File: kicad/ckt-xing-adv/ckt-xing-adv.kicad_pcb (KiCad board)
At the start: 2 copper layers, 127 x 76.2 mm, 131 parts, among them J1 Screw_Terminal_01x02, J10 SM04B-SRSS, J11 SM04B-SRSS, J12 SM04B-SRSS, J13 Conn_02x03_Row_Letter_First, J14 Conn_02x03_Row_Letter_First, J15 Conn_02x05_Counter_Clockwise, J16 SM04B-SRSS, J17 Screw_Terminal_01x02, J18 Screw_Terminal_01x02, J2 Screw_Terminal_01x02, J3 Screw_Terminal_01x02, J4 SM04B-SRSS, J5 SM04B-SRSS, J6 SM04B-SRSS, J7 SM04B-SRSS, J8 SM04B-SRSS, J9 SM04B-SRSS, Q1 ZXMS6004FF, Q2 ZXMS6004FF, Q3 ZXMS6004FF, SW1 FSM4JSMATR, SW2 FSM4JSMATR, SW3 FSM4JSMATR, U1 AP7381-33Y, U2 AP63205WU, U3 W25Q128JVS, U4 ATtiny861A-S, U5 PCA9685PW, U6 PCA9555D, U7 PAM8301, U8 DRV8231A, U9 DRV8231A

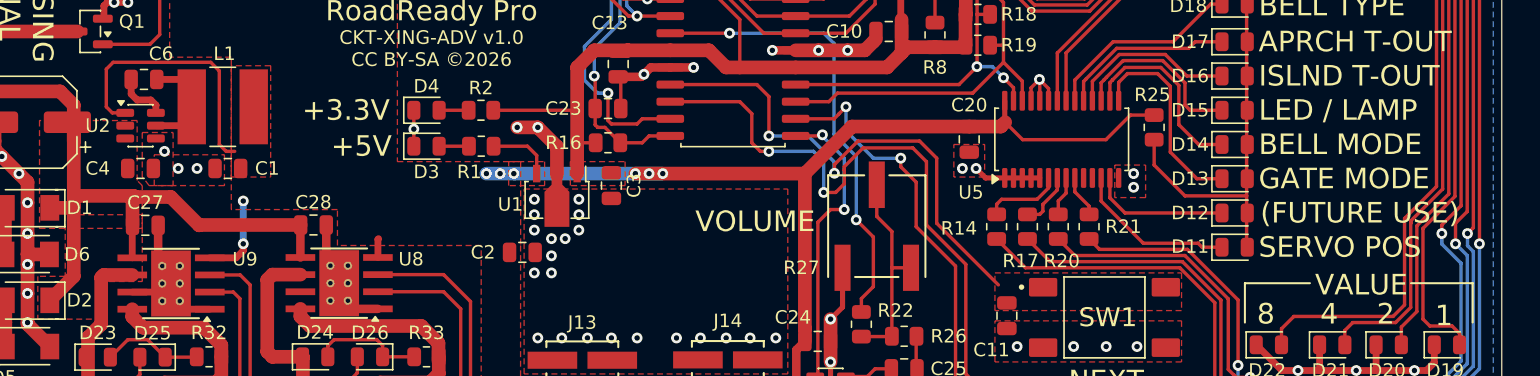
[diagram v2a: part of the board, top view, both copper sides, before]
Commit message: Updates to the big crossing - fix some actual DRC issues
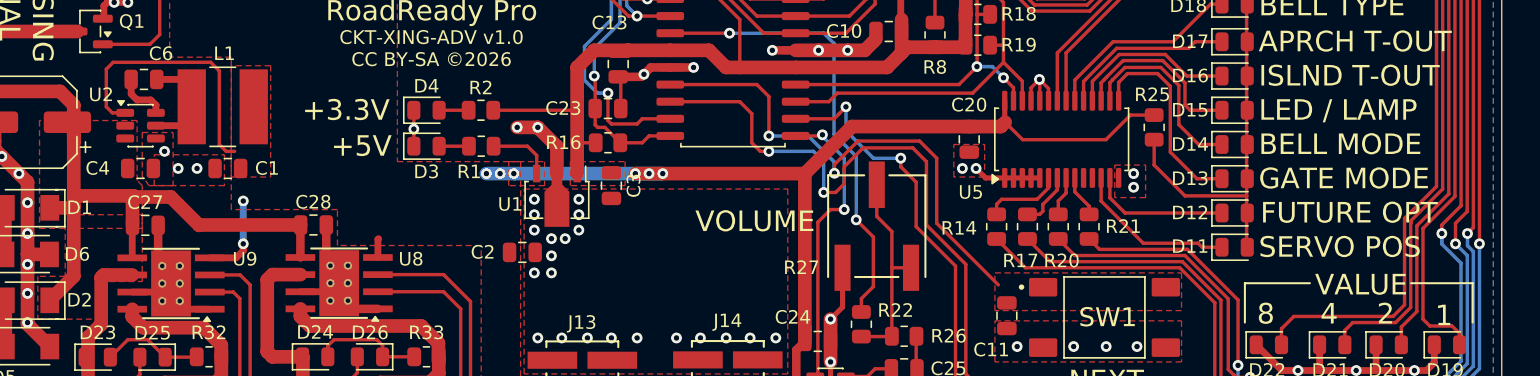
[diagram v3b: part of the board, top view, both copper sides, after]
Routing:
- net GND: track 160.5 -> 163.6 mm
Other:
- board text added: "FUTURE OPT"
- board text removed: "(FUTURE USE)"
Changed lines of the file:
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@@
 		(sheetname "/")
 		(sheetfile "ckt-xing-adv.kicad_sch")
-		(attr through_hole)
+		(attr smd)
 		(fp_line
 			(start -0.948813 2.9337)
@@
 		)
 		(embedded_fonts no)
+		(model "${ISE_3DMODELS}/Coilcraft-MSS6132.step"
+			(offset
+				(xyz 0 0 0)
+			)
+			(scale
+				(xyz 1 1 1)
+			)
+			(rotate
+				(xyz 90 -180 -90)
+			)
+		)
 	)
 	(footprint "Connector_JST:JST_SH_SM04B-SRSS-TB_1x04-1MP_P1.00mm_Horizontal"
@@
 		(sheetname "/")
 		(sheetfile "ckt-xing-adv.kicad_sch")
-		(attr through_hole)
+		(attr through_hole allow_missing_courtyard)
 		(fp_line
 			(start -2.62 3.62)
@@
 		)
 		(embedded_fonts no)
-		(model "${KICAD9_3DMODEL_DIR}/TerminalBlock_RND.3dshapes/TerminalBlock_RND_205-00012_1x02_P5.00mm_Horizontal.step"
+		(model "${ISE_3DMODELS}/Terminal_Block_2Pos_5mm.stp"
 			(offset
-				(xyz 0 0 0)
+				(xyz -2.54 -3.7338 0)
 			)
 			(scale
@@
 			)
 			(rotate
-				(xyz 0 0 0)
+				(xyz -0 -0 -0)
 			)
 		)
@@
 		(tags "TSOT TO_SOT_SMD")
 		(property "Reference" "U2"
-			(at -3.175 0 0)
+			(at -2.921 -2.286 0)
 			(layer "F.SilkS")
 			(effects
@@
 		)
 		(embedded_fonts no)
+		(model "${ISE_3DMODELS}/MOLEX_015910060.step"
+			(offset
+				(xyz 0 0 2.54)
+			)
+			(scale
+				(xyz 1 1 1)
+			)
+			(rotate
+				(xyz -90 -0 -0)
+			)
+		)
 	)
 	(footprint "LED_SMD:LED_0805_2012Metric"
@@
 		(sheetfile "ckt-xing-adv.kicad_sch")
 		(solder_mask_margin 0.07)
-		(attr smd)
 		(fp_line
 			(start -2.075 2.575)
@@
 		)
 		(embedded_fonts no)
-		(model "${KICAD9_3DMODEL_DIR}/TerminalBlock_RND.3dshapes/TerminalBlock_RND_205-00012_1x02_P5.00mm_Horizontal.step"
+		(model "${ISE_3DMODELS}/Terminal_Block_2Pos_5mm.stp"
 			(offset
-				(xyz 0 0 0)
+				(xyz -2.54 -3.7338 0)
 			)
 			(scale
@@
 			)
 			(rotate
-				(xyz 0 0 0)
+				(xyz -0 -0 -0)
 			)
 		)
@@
 		)
 		(embedded_fonts no)
+		(model "${ISE_3DMODELS}/FSM4JSMA.step"
+			(offset
+				(xyz 0 0 3.81)
+			)
+			(scale
+				(xyz 1 1 1)
+			)
+			(rotate
+				(xyz -0 -0 -90)
+			)
+		)
 	)
 	(footprint "LED_SMD:LED_0805_2012Metric"
@@
 			(layer "F.Fab")
 		)
+		(fp_circle
+			(center -2.54 -4.124999)
+			(end -2.159 -4.124999)
+			(stroke
+				(width 0.508)
+				(type solid)
+			)
+			(fill no)
+			(layer "F.Fab")
+		)
 		(fp_text user "${REFERENCE}"
 			(at 0 0 90)
@@
 		)
 		(embedded_fonts no)
+		(model "${ISE_3DMODELS}/MOLEX_015910060.step"
+			(offset
+				(xyz 0 0 2.54)
+			)
+			(scale
+				(xyz 1 1 1)
+			)
+			(rotate
+				(xyz -90 -0 -0)
+			)
+		)
 	)
 	(footprint "LED_SMD:LED_0805_2012Metric"
@@
 		(tags "THT terminal block RND 205-00012 pitch 5mm size 10x7.6mm drill 1.3mm pad 2.5mm")
 		(property "Reference" "J1"
-			(at -3.5284 -0.1316 180)
+			(at -3.5284 -0.1316 0)
 			(layer "F.SilkS")
 			(effects
@@
 		(sheetname "/")
 		(sheetfile "ckt-xing-adv.kicad_sch")
-		(attr through_hole)
+		(attr through_hole allow_missing_courtyard)
 		(fp_line
 			(start -2.62 3.62)
@@
 		)
 		(embedded_fonts no)
-		(model "${KICAD9_3DMODEL_DIR}/TerminalBlock_RND.3dshapes/TerminalBlock_RND_205-00012_1x02_P5.00mm_Horizontal.step"
+		(model "${ISE_3DMODELS}/Terminal_Block_2Pos_5mm.stp"
 			(offset
-				(xyz 0 0 0)
+				(xyz -2.54 -3.683 0)
 			)
 			(scale
@@
 			)
 			(rotate
-				(xyz 0 0 0)
+				(xyz -0 -0 -0)
 			)
 		)
@@
 		)
 		(embedded_fonts no)
-		(model "${KICAD9_3DMODEL_DIR}/TerminalBlock_RND.3dshapes/TerminalBlock_RND_205-00012_1x02_P5.00mm_Horizontal.step"
+		(model "${ISE_3DMODELS}/Terminal_Block_2Pos_5mm.stp"
 			(offset
-				(xyz 0 0 0)
+				(xyz -2.54 -3.7338 0)
 			)
 			(scale
@@
 			)
 			(rotate
-				(xyz 0 0 0)
+				(xyz -0 -0 -0)
 			)
 		)
@@
 		)
 		(embedded_fonts no)
+		(model "${ISE_3DMODELS}/FSM4JSMA.step"
+			(offset
+				(xyz 0 0 3.81)
+			)
+			(scale
+				(xyz 1 1 1)
+			)
+			(rotate
+				(xyz -0 -0 -90)
+			)
+		)
 	)
 	(footprint "ISE_UltraLibrarian:POT_3361P_BRN"
@@
 		)
 		(embedded_fonts no)
+		(model "${ISE_3DMODELS}/Bournes-3361P.step"
+			(offset
+				(xyz 1.905 -1.27 2.413)
+			)
+			(scale
+				(xyz 1 1 1)
+			)
+			(rotate
+				(xyz -0 -0 -180)
+			)
+		)
 	)
 	(footprint "Capacitor_SMD:C_0805_2012Metric"
@@
 		)
 		(embedded_fonts no)
+		(model "${ISE_3DMODELS}/FSM4JSMA.step"
+			(offset
+				(xyz 0 0 3.81)
+			)
+			(scale
+				(xyz 1 1 1)
+			)
+			(rotate
+				(xyz -0 -0 -90)
+			)
+		)
 	)
 	(footprint "Package_SO:TSSOP-28_4.4x9.7mm_P0.65mm"
@@
 		(tags "THT terminal block RND 205-00012 pitch 5mm size 10x7.6mm drill 1.3mm pad 2.5mm")
 		(property "Reference" "J2"
-			(at 7.453 -5.8825 180)
+			(at 7.453 -5.8825 0)
 			(layer "F.SilkS")
 			(effects
@@
 		)
 		(embedded_fonts no)
-		(model "${KICAD9_3DMODEL_DIR}/TerminalBlock_RND.3dshapes/TerminalBlock_RND_205-00012_1x02_P5.00mm_Horizontal.step"
+		(model "${ISE_3DMODELS}/Terminal_Block_2Pos_5mm.stp"
 			(offset
-				(xyz 0 0 0)
+				(xyz -2.54 -3.7338 0)
 			)
 			(scale
@@
 			)
 			(rotate
-				(xyz 0 0 0)
+				(xyz -0 -0 -0)
 			)
 		)
@@
 		(sheetfile "ckt-xing-adv.kicad_sch")
 		(solder_mask_margin 0.07)
-		(attr smd)
 		(fp_line
 			(start -2.075 2.575)
@@
 		)
 	)
-	(gr_text "(FUTURE USE)"
+	(gr_text "FUTURE OPT"
 		(at 134.493 70.231 0)
 		(layer "F.SilkS")
@@
 	)
 	(segment
+		(start 63.292 76.073)
+		(end 65.532 76.073)
+		(width 0.508)
+		(layer "F.Cu")
+		(net 5)
+	)
+	(segment
 		(start 68.834 40.259)
 		(end 71.501 40.259)
@@
 	)
 	(segment
+		(start 65.532 76.073)
+		(end 66.167 75.438)
+		(width 0.508)
+		(layer "F.Cu")
+		(net 5)
+	)
+	(segment
 		(start 50.4952 46.04375)
 		(end 49.4792 46.04375)
@@
 		(polygon
 			(pts
-				(xy 58.166 65.659) (xy 58.166 67.564) (xy 61.087 67.564) (xy 61.087 59.309) (xy 58.166 59.309) (xy 58.166 65.659)
+				(xy 58.166 65.659) (xy 58.166 67.564) (xy 61.087 67.564) (xy 61.087 59.309) (xy 58.166 59.309)
 			)
 		)

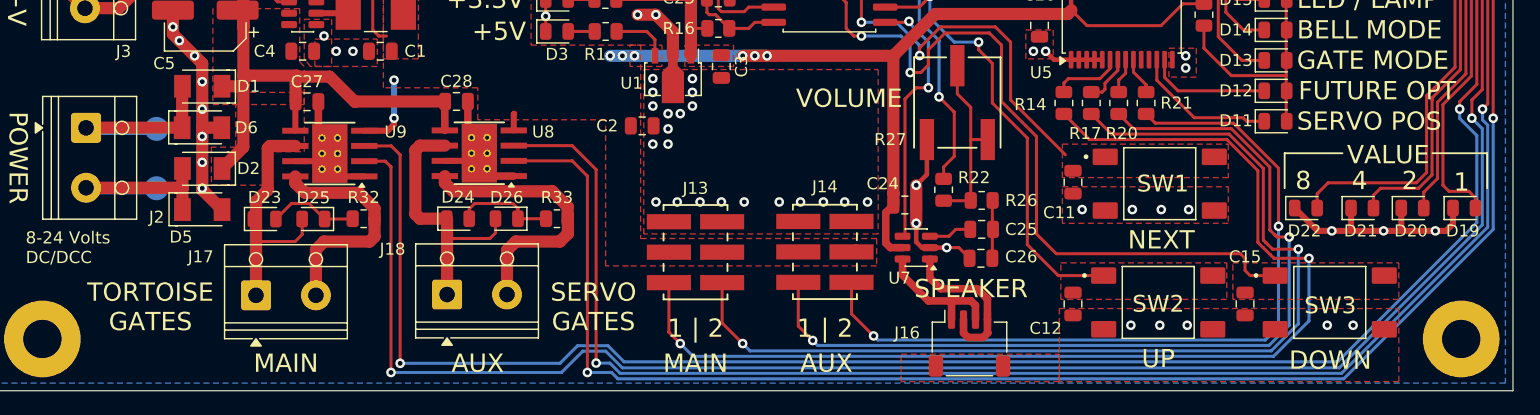
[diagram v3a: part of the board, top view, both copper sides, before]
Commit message: Add test points for servo outputs Feedback from Michael on text position, etc
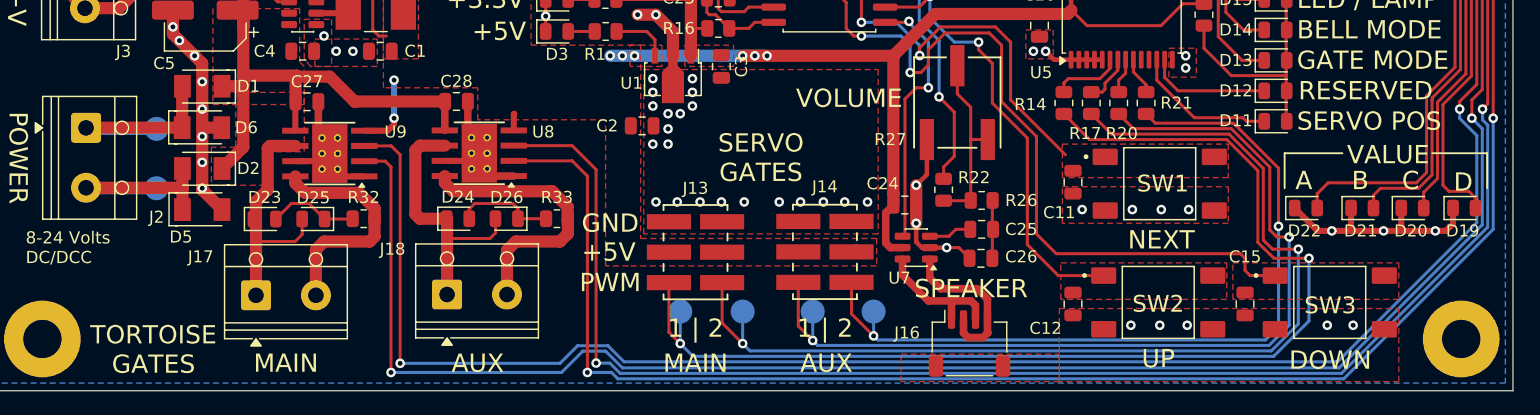
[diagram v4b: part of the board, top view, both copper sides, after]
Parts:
- added TP6: TestPoint, TestPoint:TestPoint_Pad_D2.0mm, B.Cu at (82.9, 88.6)
- added TP7: TestPoint, TestPoint:TestPoint_Pad_D2.0mm, B.Cu at (88.1, 88.6)
- added TP8: TestPoint, TestPoint:TestPoint_Pad_D2.0mm, B.Cu at (94.0, 88.6)
- added TP9: TestPoint, TestPoint:TestPoint_Pad_D2.0mm, B.Cu at (99.1, 88.6)
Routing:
- net Net-(J13-Pin_b1): track 85.0 -> 87.7 mm
- net Net-(J13-Pin_a1): track 93.8 -> 96.4 mm
- net Net-(J14-Pin_a1): track 74.9 -> 77.3 mm
- net Net-(J14-Pin_b1): track 65.8 -> 67.8 mm
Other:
- board text added: "A"
- board text added: "B"
- board text added: "D"
- board text added: "GND"
- board text added: "PWM"
- board text added: "RESERVED"
- board text removed: "1"
- board text removed: "2"
- board text removed: "4"
- board text removed: "8"
- board text removed: "FUTURE OPT"
